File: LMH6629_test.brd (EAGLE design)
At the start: 50 x 50 mm, 6 parts, among them X1 1-227161-0

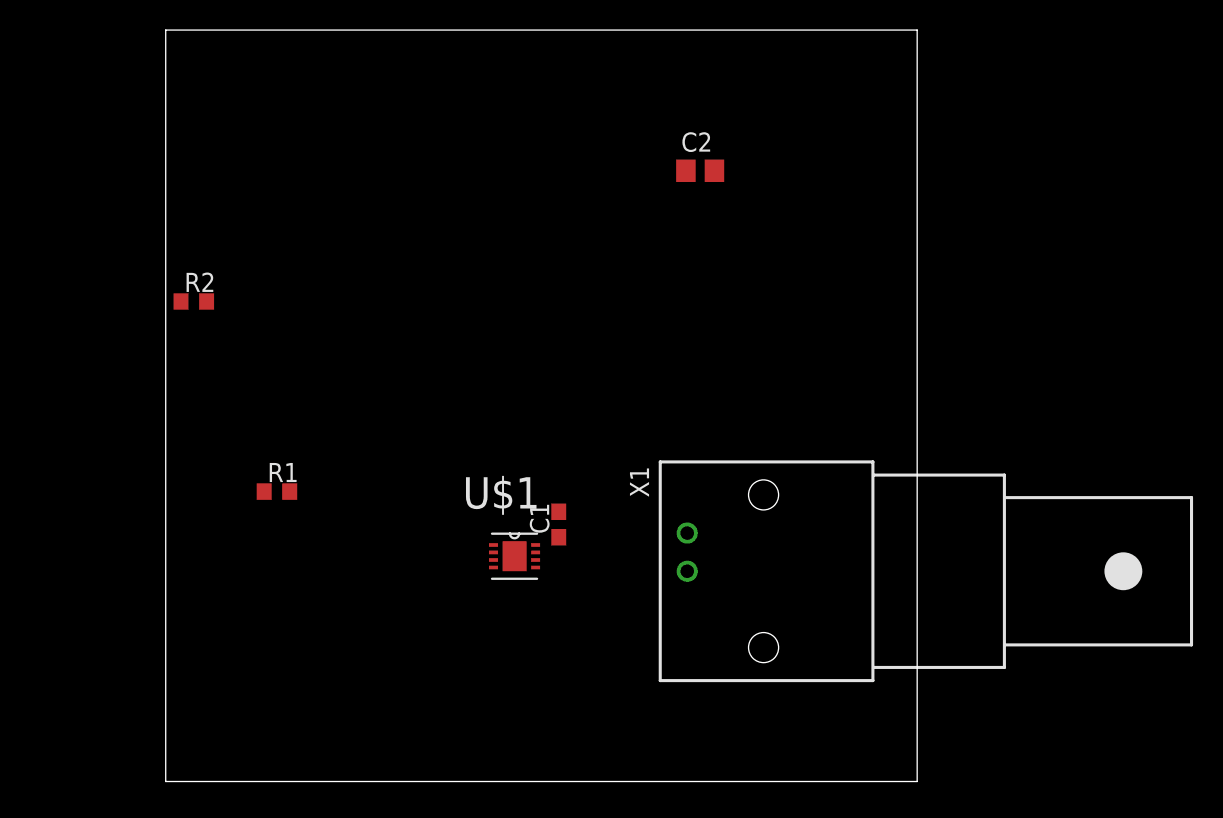
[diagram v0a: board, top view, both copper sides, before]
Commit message: add NCP5661
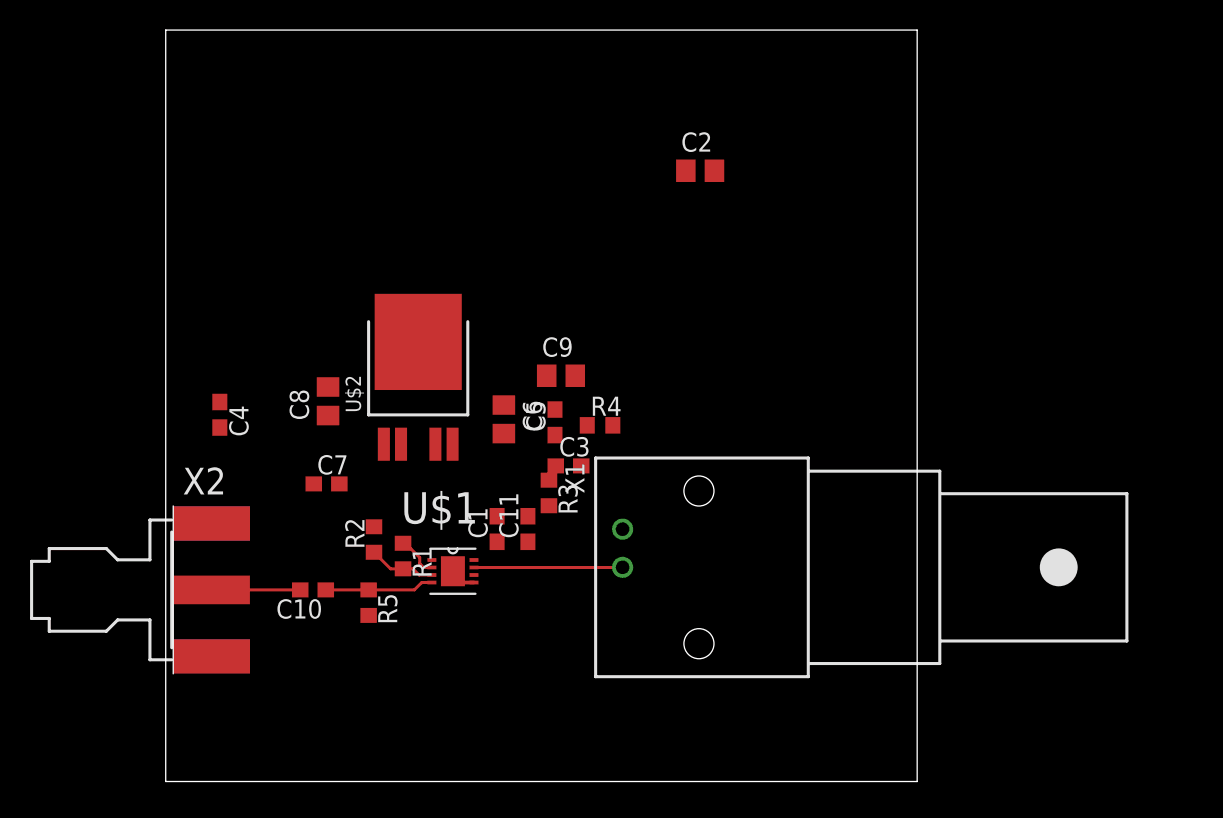
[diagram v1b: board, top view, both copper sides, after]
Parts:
- added C10, C11, C3, C4, C5, C7: (no value), rcl:C0603
- added C6, C8, C9: (no value), rcl:C0805
- added R3, R4, R5: (no value), resistor:R0603
- added U$2: NCP5661DTADJRKG, on-semi:DPAK-5
- added X2: SMA-142-0711-871/876, con-coax:J502-ND-142-0711-871/876
- moved R2 19.9 mm to (13.9, 16.1), turned to 90 degrees
- moved R1 9.42 mm to (15.8, 15.0), turned to 270 degrees
- moved X1 4.31 mm to (35.5, 14.2)
- moved U$1 4.22 mm to (19.1, 14.0)
- moved C1 4.11 mm to (22.1, 16.8)
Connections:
- net N$1 renamed V_OUT
- removed net N$3: C1.1, U$1.8
- new net IN: C10.2, X2.1
- new net N$4: R3.1, R4.2, U$2.5
- new net N$5: R1.2, R2.1, U$1.3
- new net N$6: R1.1, U$1.2
- new net PWR_IN: C2.1, C4.1, C7.1, C8.1, U$2.1, U$2.2
- new net V_ANALOG: C1.1, C11.1, C3.1, C5.1, C6.1, C9.1, R3.2, U$1.6, U$1.8, U$2.4
- new net V_IN: C10.1, R5.1, U$1.4
- net GND: now also C11.2, C2.2, C3.2, C4.2, C5.2, C6.2, C7.2, C8.2, C9.2, R2.2, R4.1, R5.2, U$2.3, X2.G@1, X2.G@2, X2.G@3, X2.G@4
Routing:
- net V_OUT: track 0.00 -> 9.89 mm
- net V_IN: track 0.00 -> 7.26 mm
- net IN: track 0.00 -> 5.88 mm
- net N$5: track 0.00 -> 4.48 mm
- net N$6: track 0.00 -> 2.82 mm
- net GND: track 0.00 -> 1.71 mm

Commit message: some progress on pcb
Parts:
- removed C5: (no value), rcl:C0603
- removed C9: (no value), rcl:C0805
- moved C2 31.7 mm to (9.16, 23.1), turned to 90 degrees
- moved C4 7.45 mm to (10.9, 22.9), turned to 90 degrees
- moved C6 6.89 mm to (19.5, 17.9), turned to 0 degrees
- moved C3 6.71 mm to (23.1, 15.4), turned to 90 degrees
- moved C11 5.20 mm to (19.6, 19.4), turned to 0 degrees
- moved R3 5.02 mm to (22.1, 22.9), turned to 180 degrees
- moved C8 4.30 mm to (7.10, 23.1)
- moved R4 3.49 mm to (25.5, 22.9), turned to 180 degrees
- moved C7 3.49 mm to (12.3, 22.9), turned to 90 degrees
- moved C1 1.43 mm to (21.8, 15.4)
- moved X2 0.98 mm to (0.90, 11.8)
- moved R2 0.90 mm to (13.9, 15.2)
- moved U$2 0.90 mm to (16.8, 28.4)
- moved C10 0.90 mm to (9.80, 11.8)
- moved R1 0.90 mm to (15.8, 14.1)
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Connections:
- net N$4 renamed ADJ
- net GND: no longer C5.2, C9.2
- net V_ANALOG: no longer C5.1, C9.1
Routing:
- net ADJ: track 0.00 -> 6.68 mm
- net V_ANALOG: track 0.00 -> 4.48 mm
- added copper zone on layer 1, net GND
- added copper zone on layer 1, net PWR_IN
- added copper zone on layer 1, net V_ANALOG
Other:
- board size 50 x 50 mm -> 43 x 35 mm

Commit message: more progress on pcb
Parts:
- moved C3 5.77 mm to (17.4, 16.3), turned to 180 degrees
- moved C1 0.79 mm to (21.0, 15.7), turned to 0 degrees
- moved X2 0.40 mm to (0.50, 11.8)
- moved C11 0.22 mm to (19.5, 19.6)
- moved C6 0.14 mm to (19.4, 18.0)
- moved C8 0.10 mm to (7.10, 23.0)
- moved C2 0.08 mm to (9.10, 23.0)
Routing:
- net V_ANALOG: track 4.48 -> 8.56 mm, vias 0 -> 2
- net GND: vias 0 -> 38
- added copper zone on layer 16, net GND

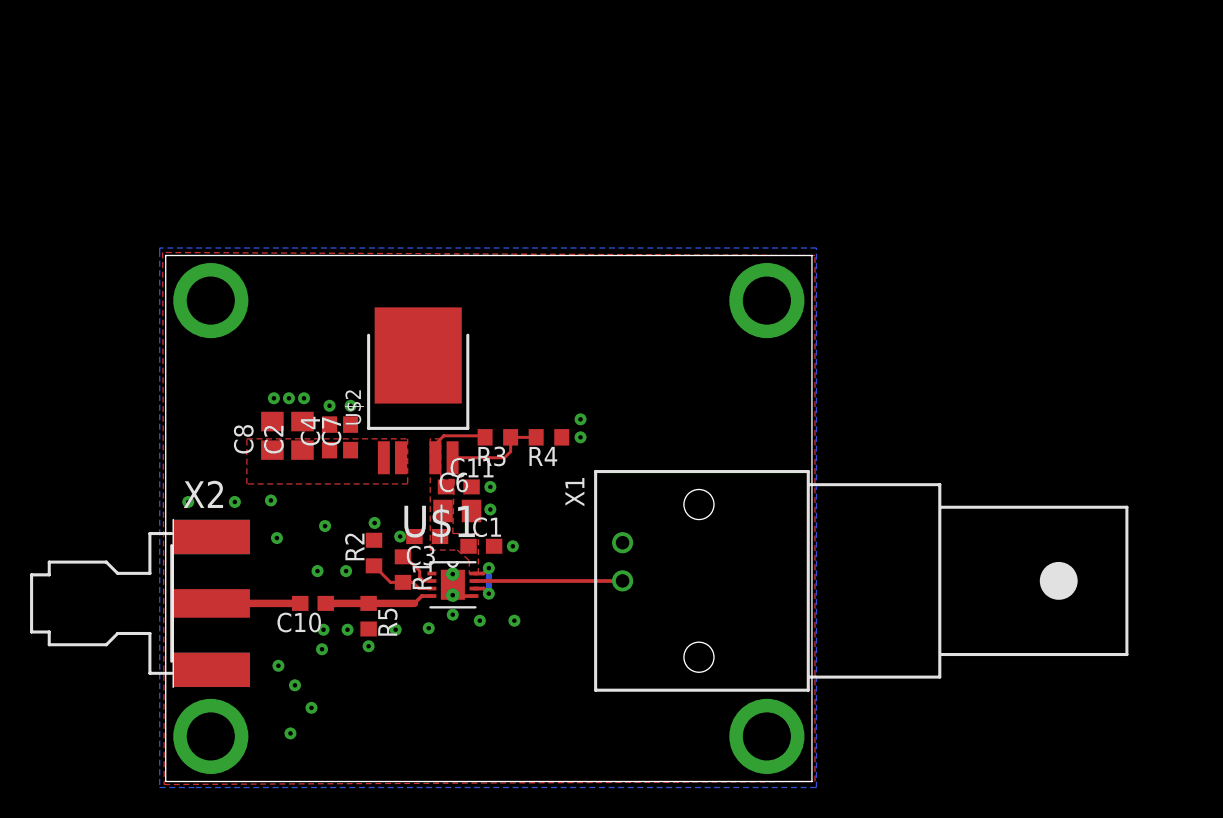
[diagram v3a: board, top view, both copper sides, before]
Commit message: replace LDO on pcb
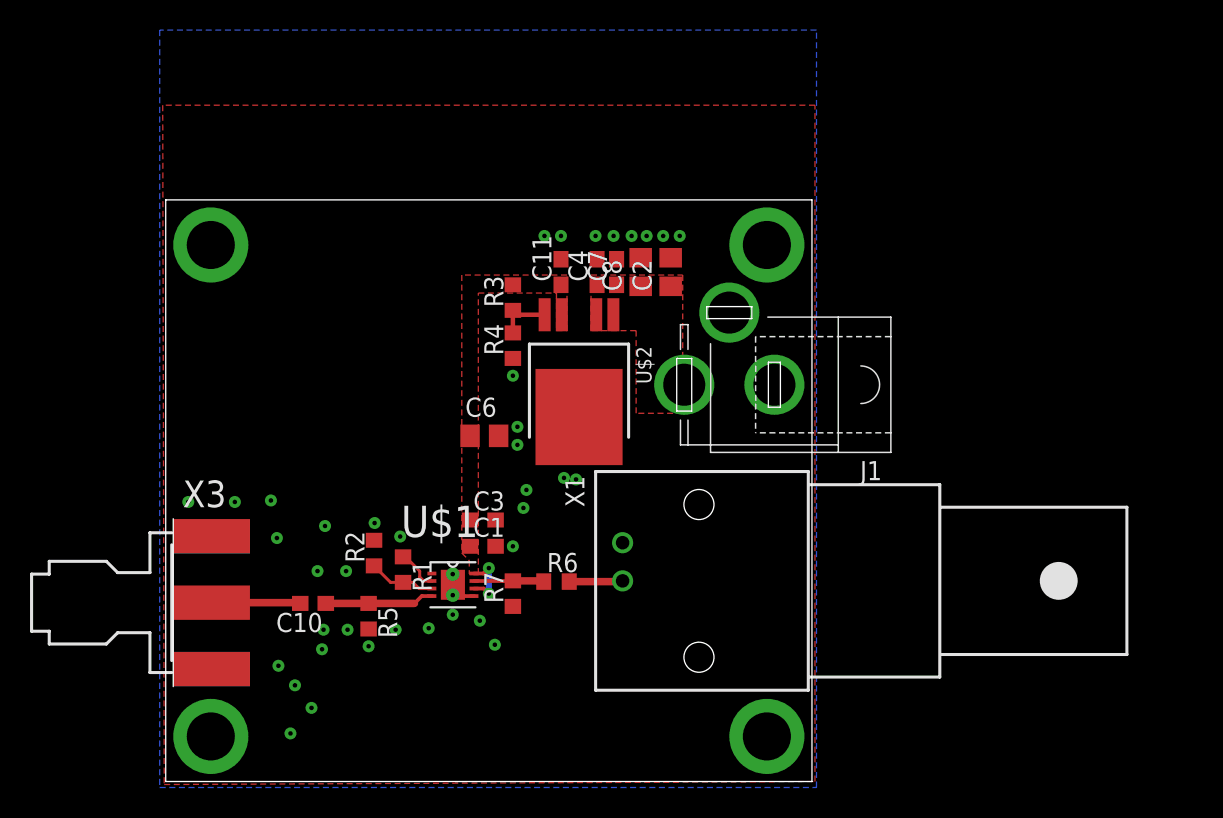
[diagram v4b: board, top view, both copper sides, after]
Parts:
- removed X2: SMA-142-0711-871/876, con-coax:J502-ND-142-0711-871/876
- added J1: (no value), con-jack:SPC4078
- added R6, R7: (no value), resistor:R0603
- added X3: SMA-142-0701-801/806, con-coax:J502-ND-142-0701-801/806
- moved C2 26.8 mm to (33.6, 33.9)
- moved C8 26.8 mm to (31.6, 33.9)
- moved C4 20.9 mm to (28.7, 33.9)
- moved C7 20.8 mm to (30.0, 33.9)
- moved C11 15.8 mm to (26.3, 33.9), turned to 90 degrees
- moved U$2 11.5 mm to (27.5, 24.2), turned to 180 degrees
- moved R3 9.35 mm to (23.1, 32.2), turned to 90 degrees
- moved R4 6.56 mm to (23.1, 29.0), turned to 90 degrees
- moved C6 5.31 mm to (21.2, 23.0)
- moved C3 3.86 mm to (21.1, 17.4), turned to 0 degrees
- moved C1 0.10 mm to (21.1, 15.7)
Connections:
- removed net IN: C10.2, X2.1
- removed net V_OUT: U$1.7, X1.1
- new net N$1: R6.1, R7.2, U$1.7
- new net N$2: R6.2, X1.1
- new net N$3: C10.2, X3.1
- net GND: now also J1.1, J1.2, R7.1, X3.G@1, X3.G@2, X3.G@3, X3.G@4; no longer X2.G@1, X2.G@2, X2.G@3, X2.G@4
- net PWR_IN: now also J1.3
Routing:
- net V_OUT: track 9.89 -> 0.00 mm
- net N$3: track 0.00 -> 5.91 mm
- net IN: track 5.88 -> 0.00 mm
- net N$1: track 0.00 -> 4.66 mm
- net V_ANALOG: track 8.56 -> 4.08 mm
- net N$2: track 0.00 -> 3.57 mm
- net ADJ: track 6.68 -> 3.73 mm
- net GND: vias 38 -> 44
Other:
- board size 43 x 35 mm -> 43 x 38.7 mm

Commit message: almost done with pcb
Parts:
- removed J1: (no value), con-jack:SPC4078
- added C5: (no value), rcl:C0603
- added LED1: (no value), adafruit:CHIPLED_0603
- added R8: (no value), resistor:R0603
- added X2: (no value), adafruit:SMA_EDGELAUNCH
- R1, R2: device resistor:R0603 -> resistor:R0402
- R6, R7: value (none) -> 51R
- X3: value SMA-142-0701-801/806 -> (none); device con-coax:J502-ND-142-0701-801/806 -> con-jack:SPC4078
- moved X3 39.9 mm to (37.5, 26.7), turned to 180 degrees
- moved R2 2.56 mm to (16.0, 13.8)
- moved R1 1.42 mm to (14.5, 14.7)
- moved C2 0.50 mm to (34.1, 33.9)
- moved C8 0.50 mm to (32.1, 33.9)
- moved C7 0.30 mm to (30.3, 33.9)
- moved C3 0.10 mm to (21.1, 17.3)
- renumbered U$1 to U1, U$2 to U2
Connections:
- net N$1 renamed V_OUT
- net N$2 renamed OUT
- net N$5 renamed -IN
- removed net N$6: R1.1, U1.2
- new net FB: R2.2, U1.2
- new net N$1: LED1.A, R8.1
- net GND: now also C5.2, LED1.C, R1.1, X2.GND@1, X2.GND@2, X2.GND@3, X2.GND@4, X3.1, X3.2; no longer J1.1, J1.2, R2.2, X3.G@1, X3.G@2, X3.G@3, X3.G@4
- net N$3: now also X2.P; no longer X3.1
- net PWR_IN: now also X3.3; no longer J1.3
- net V_ANALOG: now also C5.1, R8.2
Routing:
- net N$6: track 2.82 -> 0.00 mm
- net FB: track 0.00 -> 2.17 mm
- net N$1: track 0.00 -> 1.80 mm
- net -IN: track 4.48 -> 3.71 mm
- net N$3: track 5.91 -> 6.44 mm
- net GND: vias 44 -> 179
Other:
- board text added: "LMH6629 test pcb"

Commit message: all done
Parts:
- removed C2: (no value), rcl:C0805
- added C12: 22u, rcl:C0805
- added C13: 47u, resistor:C1210
- added C9: 51p, rcl:C0603
- C1: value (none) -> 0.01u
- C10: value (none) -> 1n
- C11, C4: value (none) -> 0.1u
- C3: value (none) -> 0.22u
- C5, C7: value (none) -> 1u
- C6: value (none) -> 4.7u
- C8: value (none) -> 10u
- R1, R8: value (none) -> 680R
- R2: value (none) -> 12R
- R3: value (none) -> 18k
- R4: value (none) -> 6.2k
- R5: value (none) -> 2.7k
- R7: value 51R -> 51R DNI
- moved C6 11.6 mm to (24.4, 34.1), turned to 90 degrees
- moved C8 9.30 mm to (32.1, 24.6), turned to 270 degrees
- moved R3 2.28 mm to (21.1, 31.1), turned to 180 degrees
- moved R4 2.05 mm to (21.9, 27.3)
- moved R1 1.75 mm to (16.0, 13.8), turned to 90 degrees
- moved R2 1.75 mm to (14.5, 14.7), turned to 270 degrees
- moved C11 0.20 mm to (26.3, 34.1)
- moved C7 0.20 mm to (30.5, 33.9)
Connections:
- net -IN: now also R1.1, R2.2; no longer R1.2, R2.1
- net ADJ: now also C9.1
- net FB: now also R1.2; no longer R2.2
- net GND: now also C12.2, C13.2, R2.1; no longer C2.2, R1.1
- net PWR_IN: now also C13.1; no longer C2.1
- net V_ANALOG: now also C12.1, C9.2
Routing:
- net ADJ: track 3.73 -> 6.27 mm
- net GND: vias 179 -> 180
